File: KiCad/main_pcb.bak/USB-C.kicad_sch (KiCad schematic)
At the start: 13 parts, among them J4 1x1 Header, J5 1x1 Header, J6 TYPE-C-31-M-12, U2 CH340C, U3 JSMSEMI AMS1117-3.3V

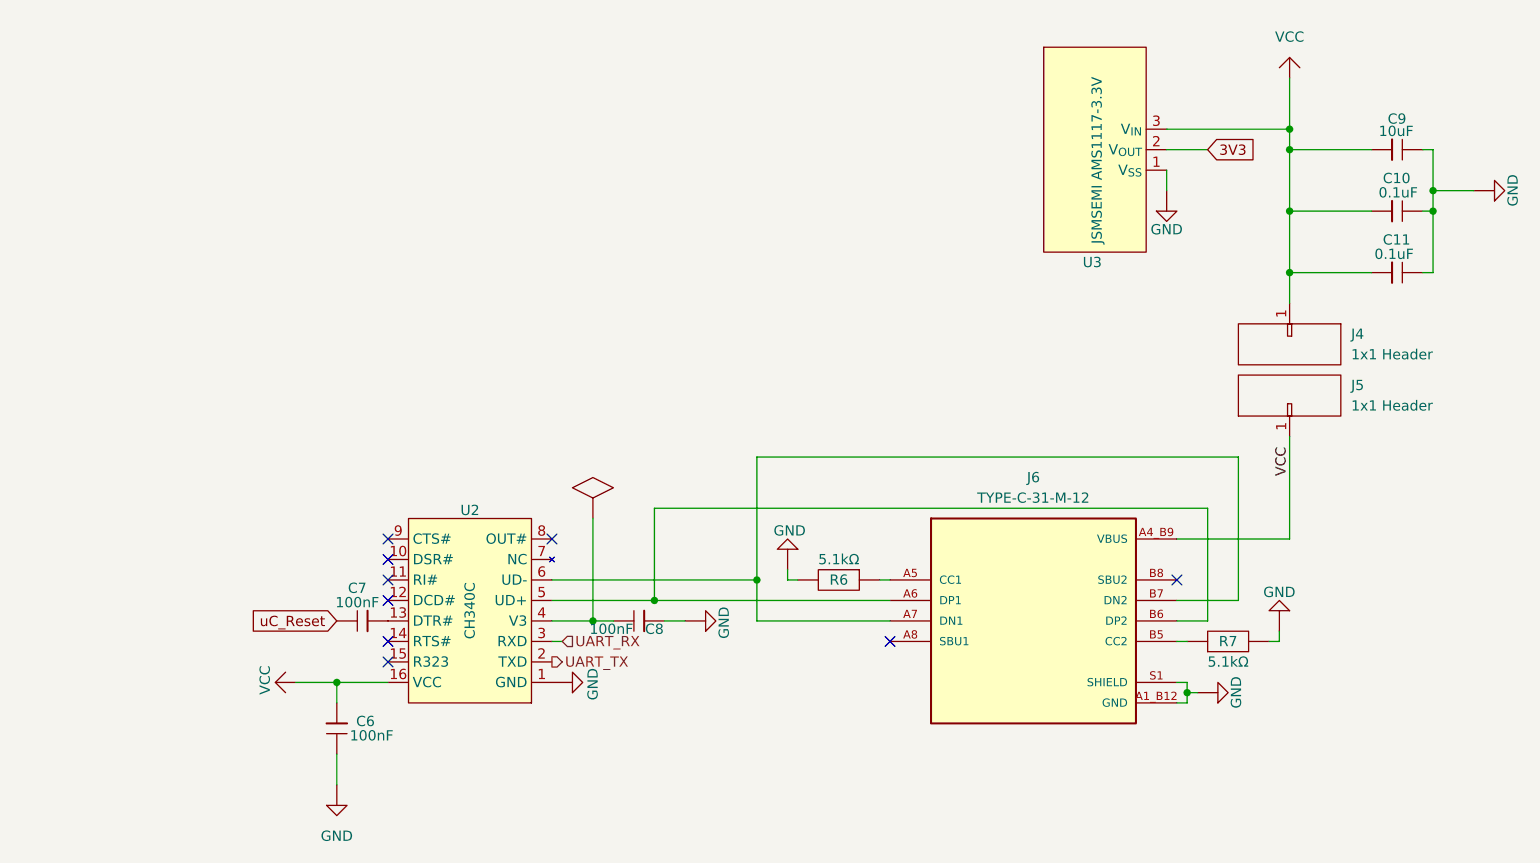
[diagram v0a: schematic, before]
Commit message: Maddie/main pcb refactor (#39)
* feat(PCB Layout): Refactors Main PCB layout to achieve smaller form factor and adds JLCPCB constraints.

* feat(symbols): Adds 4pin crystal symbols and adds it to schematic

* feat(schematic): Connects C2 and C3 to the crystal

* feat(schematic): Revamps fully the circuit schematic

* feat(schematic): Assigns footprints to symbols

* feat(pcb): Alternative first draft

* feat(pcb): Second draft

* feat(pdf): Updates schematic PDF

* feat(pdf): Updates schematic PDF

* chore(migration): Puts old layout in main_pcb.bak/ and new layout to main_pcb/

* feat(PCB): Updates PCB layout after Christian's review, thansk a lot Christian :) !
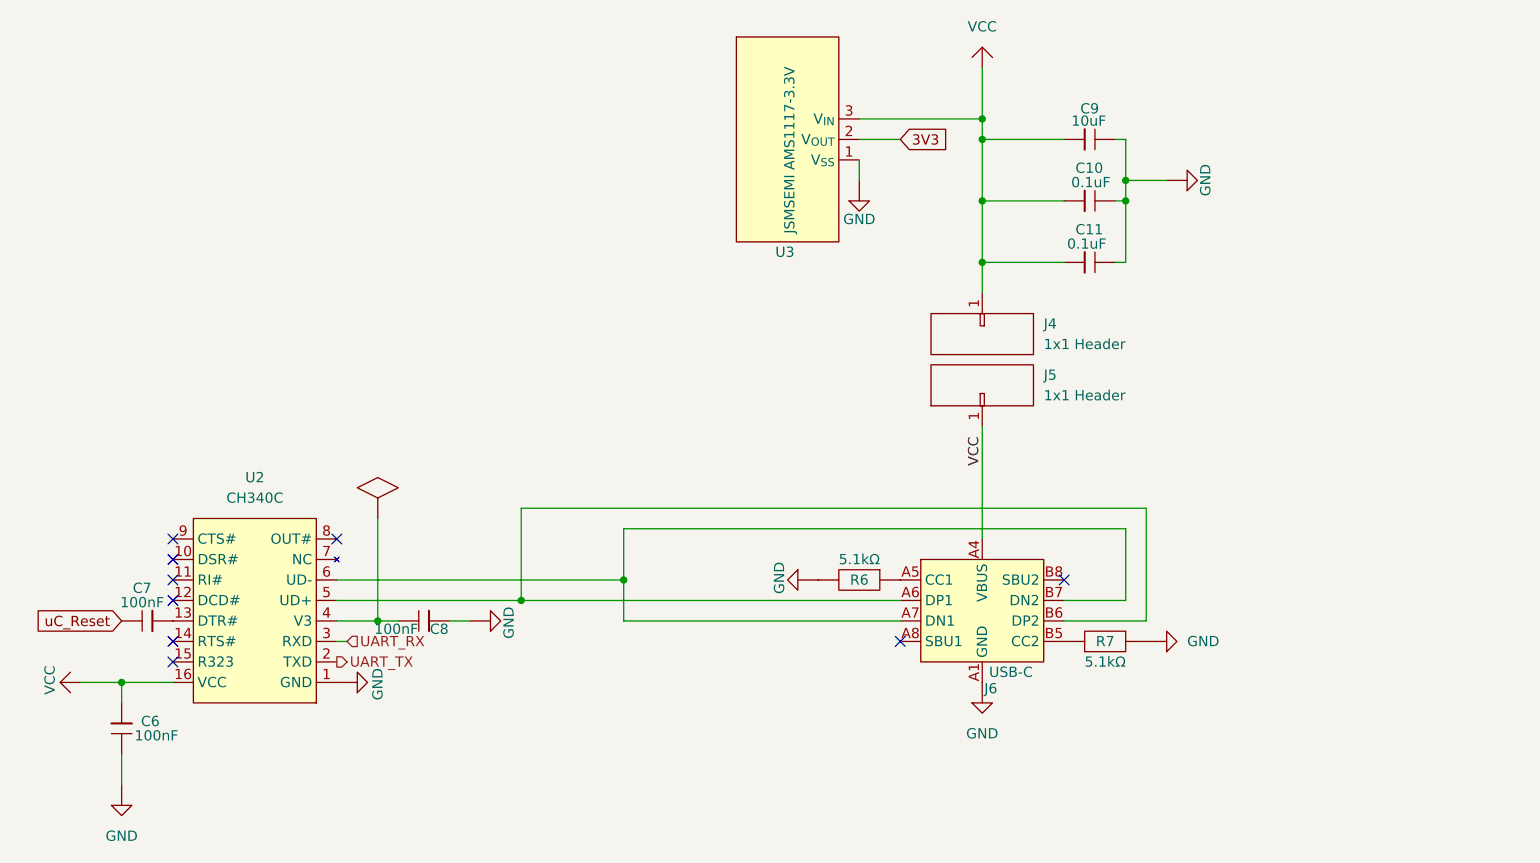
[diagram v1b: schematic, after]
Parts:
- removed J6: TYPE-C-31-M-12, Lilibrary:HRO_TYPE-C-31-M-12, symbol Lily's Pad:TYPE-C-31-M-12
- added J6: USB-C, Lilibrary:HRO_TYPE-C-31-M-12, symbol Lily's Pad:USB_TYPE-C-31-M-14
- C10, C11, C6, C7, C8, C9: footprint Capacitor_SMD:C_0603_1608Metric_Pad1.08x0.95mm_HandSolder -> Capacitor_SMD:C_0201_0603Metric_Pad0.64x0.40mm_HandSolder
- R6, R7: footprint Resistor_SMD:R_0603_1608Metric_Pad0.98x0.95mm_HandSolder -> Resistor_SMD:R_0201_0603Metric_Pad0.64x0.40mm_HandSolder
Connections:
- net GND: now also J6.A1 (GND), J6.A12 (GND), J6.B1 (GND), J6.B12 (GND)
- net VBUS: now also J6.A4 (VBUS), J6.A9 (VBUS), J6.B4 (VBUS), J6.B9 (VBUS)
- net at U2.5 (UD+): now also J6.A6 (DP1), J6.B6 (DP2)
- net at U2.6 (UD-): now also J6.A7 (DN1), J6.B7 (DN2)
- net at R7.1: now also J6.B5 (CC2)
- net at R6.1: now also J6.A5 (CC1)
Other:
- moved on the sheet: C10, C11, C6, C7, C8, C9, J4, J5, R6, R7, U2, U3
